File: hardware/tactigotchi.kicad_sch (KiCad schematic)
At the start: 33 parts, among them Q1 BC337, Q2 BC337, SW1 SW_Push, SW10 SW_SPDT, SW2 SW_Push, SW3 SW_Push, SW4 SW_Push, SW5 SW_Push, SW6 SW_Push, SW7 SW_Push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

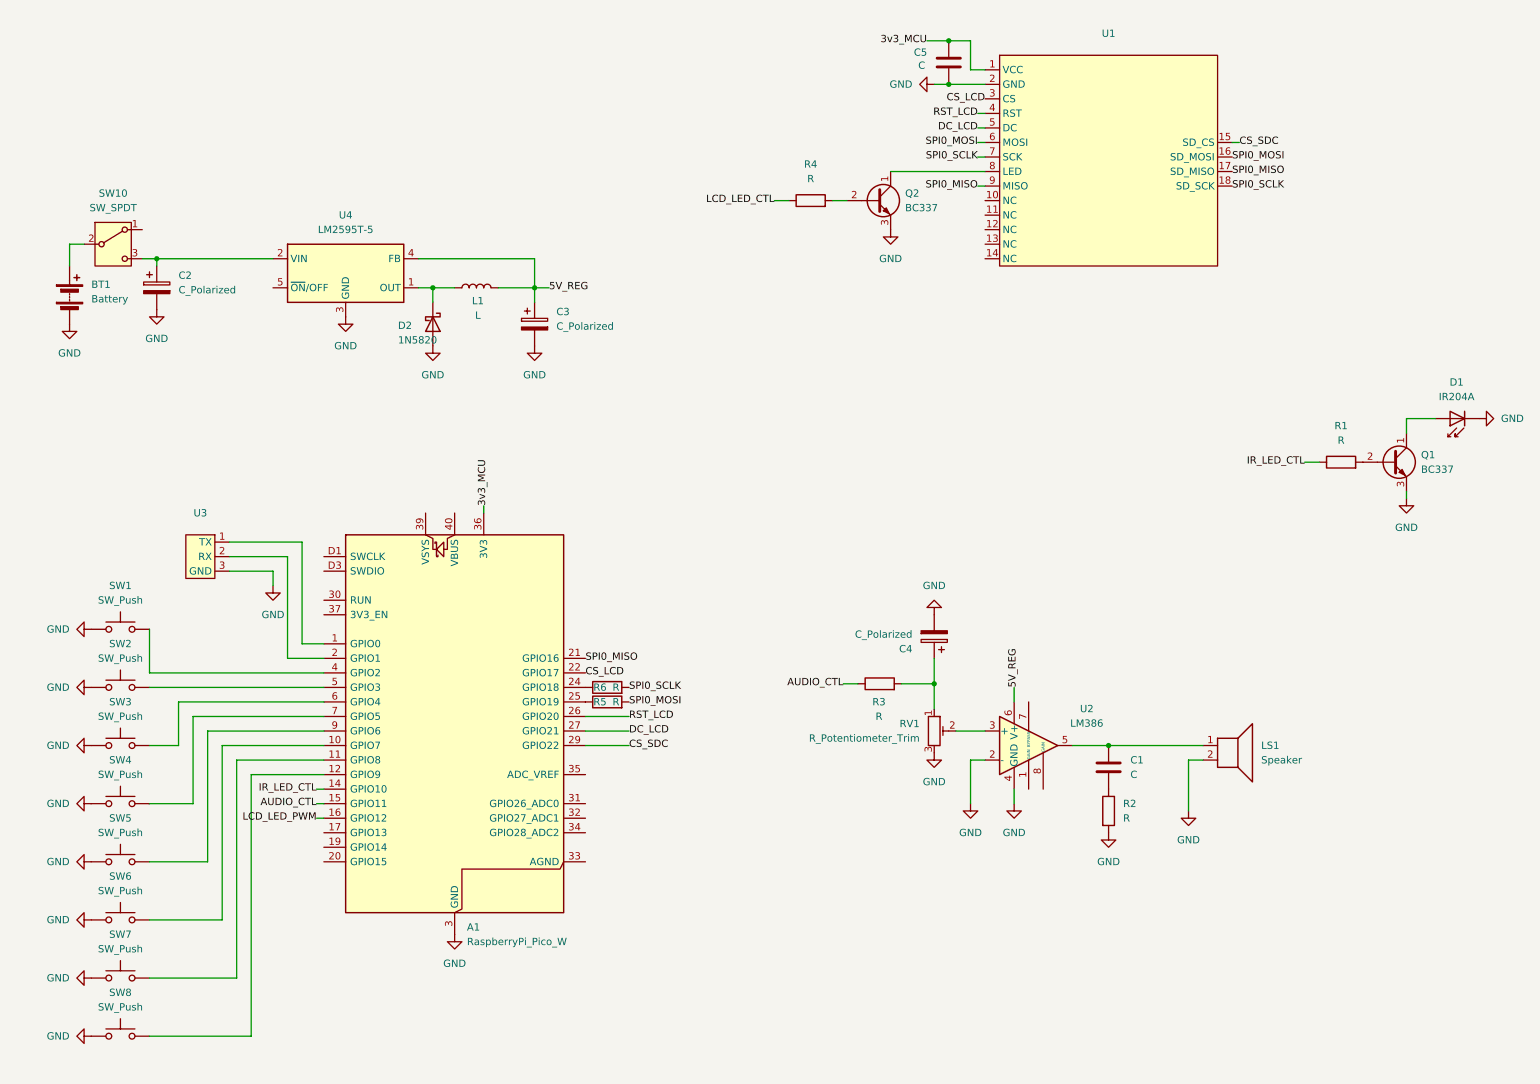
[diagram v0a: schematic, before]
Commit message: Add files via upload
smd schematic drop-in replacements, changes to psu module
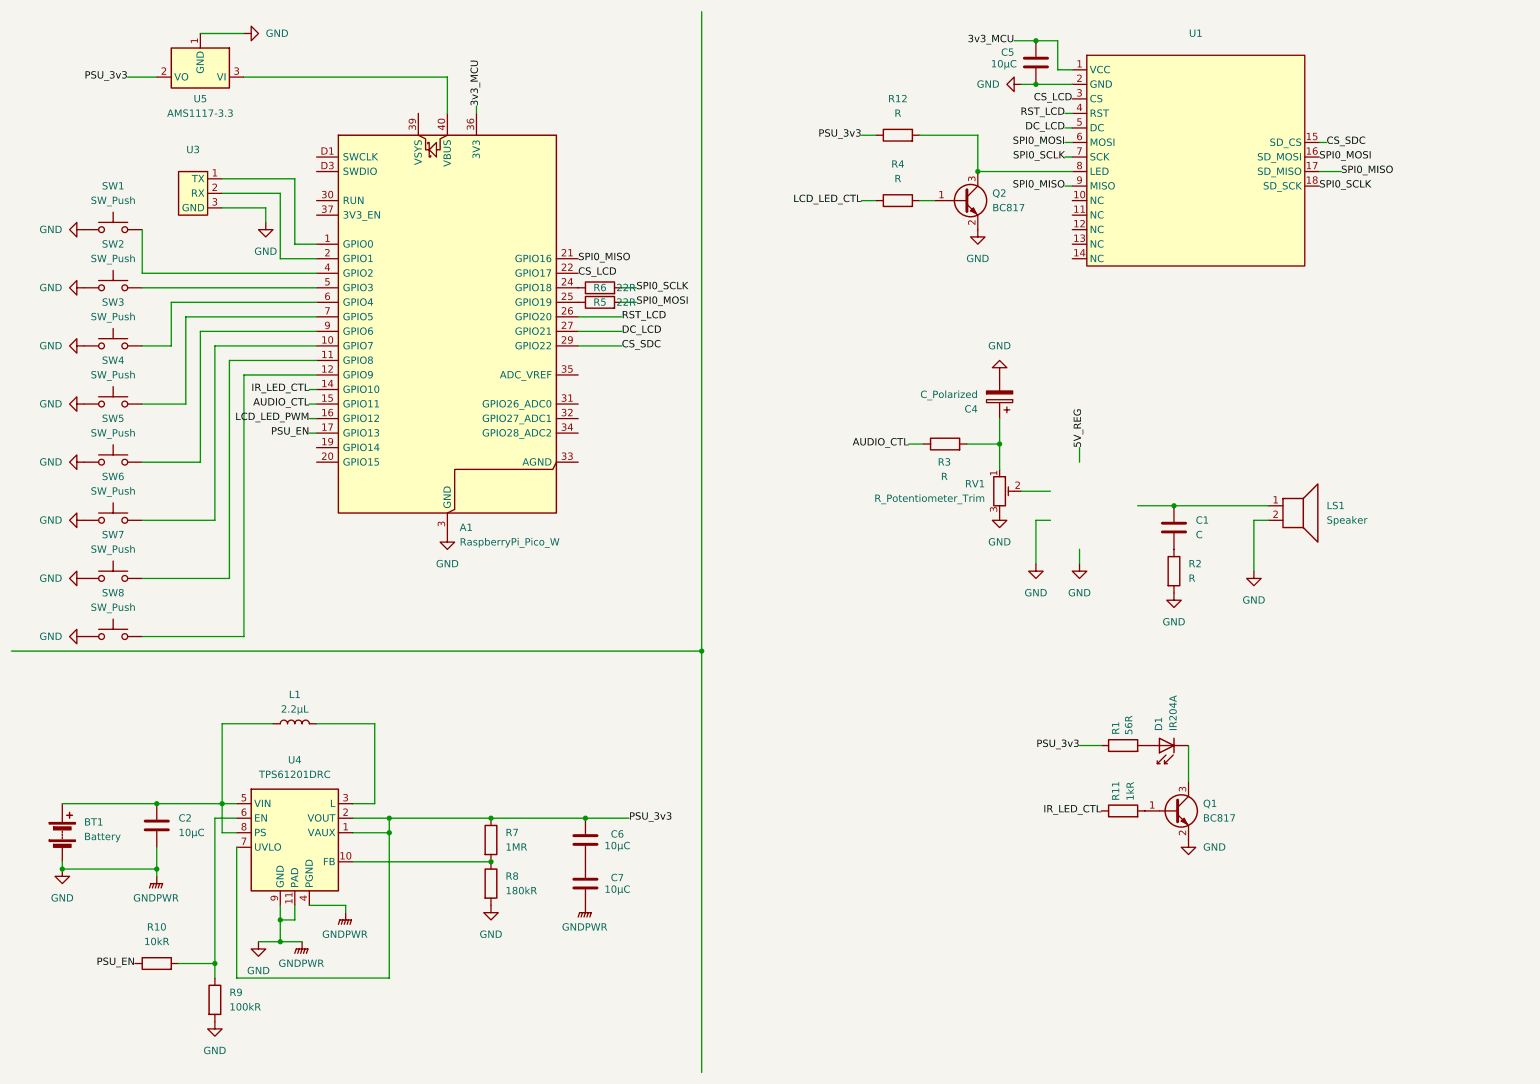
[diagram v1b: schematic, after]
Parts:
- removed C2, C3: C_Polarized, Capacitor_THT:CP_Radial_D5.0mm_P2.50mm, symbol Device:C_Polarized
- removed D2: 1N5820, Diode_THT:D_DO-201AD_P15.24mm_Horizontal, symbol Diode:1N5820
- removed Q1, Q2: BC337, Package_TO_SOT_THT:TO-92_Inline, symbol Transistor_BJT:BC337
- removed SW10: SW_SPDT, Button_Switch_THT:SW_E-Switch_EG1271_SPDT, symbol Switch:SW_SPDT
- removed U2: LM386, Package_DIP:DIP-8_W7.62mm, symbol Amplifier_Audio:LM386
- removed U4: LM2595T-5, Package_TO_SOT_THT:TO-220-5_P3.4x3.7mm_StaggerOdd_Lead3.8mm_Vertical, symbol Regulator_Switching:LM2595T-5
- added C2, C6, C7: 10μC, symbol Device:C
- added Q1, Q2: BC817, Package_TO_SOT_SMD:SOT-23, symbol Transistor_BJT:BC817
- added R10: 10kR, symbol Device:R
- added R11: 1kR, Resistor_THT:R_Axial_DIN0204_L3.6mm_D1.6mm_P5.08mm_Horizontal, symbol Device:R
- added R12: R, Resistor_THT:R_Axial_DIN0204_L3.6mm_D1.6mm_P5.08mm_Horizontal, symbol Device:R
- added R7: 1MR, symbol Device:R
- added R8: 180kR, symbol Device:R
- added R9: 100kR, symbol Device:R
- added U4: TPS61201DRC, Package_SON:Texas_S-PVSON-N10_ThermalVias, symbol Regulator_Switching:TPS61201DRC
- added U5: AMS1117-3.3, Package_TO_SOT_SMD:SOT-223-3_TabPin2, symbol Regulator_Linear:AMS1117-3.3
- C5: value C -> 10μC
- L1: value L -> 2.2μL; footprint Inductor_SMD:L_6.3x6.3_H3 -> (none)
- R1: value R -> 56R
- R5, R6: value R -> 22R
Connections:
- net 5V_REG: no longer L1.2
- net GND: now also C2.2, C7.1, Q1.2 (E), Q2.2 (E), R8.2, R9.2, U4.11 (PAD), U4.4 (PGND), U4.9 (GND), U5.1 (GND); no longer D1.1 (K)
- net IR_LED_CTL: now also R11.1; no longer R1.1
- net at R4.2: now also Q2.1 (B)
- net at U1.8 (LED): now also Q2.3 (C), R12.2
- net at R1.2: now also D1.2 (A)
- net at L1.1: now also BT1.1 (+), C2.1, U4.5 (VIN), U4.8 (PS)
- net PSU_EN: now reaches A1.17 (GPIO13)
- net PSU_EN: now also R10.1
- net at A1.40 (VBUS): now also U5.3 (VI)
- new net: Q1.1 (B), R11.2
- new net: D1.1 (K), Q1.3 (C)
- new net: R10.2, R9.1, U4.6 (EN)
- new net: C6.1, C7.2
- new net: R7.2, R8.1, U4.10 (FB)
- new net: L1.2, U4.3 (L)
- new net PSU_3v3: C6.2, R1.1, R12.1, R7.1, U4.1 (VAUX), U4.2 (VOUT), U4.7 (UVLO), U5.2 (VO)
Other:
- moved on the sheet: A1, BT1, C1, C4, C5, D1, LS1, R1, R2, R3, R4, R5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

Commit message: Add files via upload
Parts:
- removed C1: C, Capacitor_THT:CP_Radial_D5.0mm_P2.50mm, symbol Device:C
- removed C4: C_Polarized, Capacitor_THT:CP_Radial_D5.0mm_P2.50mm, symbol Device:C_Polarized
- removed R3: R, Resistor_THT:R_Axial_DIN0204_L3.6mm_D1.6mm_P5.08mm_Horizontal, symbol Device:R
- removed RV1: R_Potentiometer_Trim, Potentiometer_THT:Potentiometer_Piher_PT-10-H01_Horizontal, symbol Device:R_Potentiometer_Trim
- added C10, C8, C9: .1μC, symbol Device:C
- added C11: 22μC, symbol Device:C
- added C12: 10μC, symbol Device:C
- added R14: 22R, symbol Device:R
- added U2: PAM8302AAD, symbol Amplifier_Audio:PAM8302AAD
- R2: value R -> 1kR
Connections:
- net LCD_LED_PWM is gone; now on net LCD_LED_CTL: A1.16 (GPIO12)
- net AUDIO_CTL: now also A1.31 (GPIO26_ADC0), C8.1; no longer A1.15 (GPIO11)
- net GND: now also C10.1, C11.2, C12.2, C9.2, U2.7 (GND); no longer LS1.2
- net PSU_3v3: now also C10.2, C11.1, U2.6 (VDD)
- net SPI0_MISO: now also R14.2; no longer U1.17 (SD_MISO)
- net at A1.40 (VBUS), U5.3 (VI): now also C12.1
- net AUDIO_EN: now reaches R2.1
- net AUDIO_EN: now also A1.15 (GPIO11), U2.1 (~{SD})
- net at LS1.1: now also U2.5 (OUT+)
- new net: C8.2, U2.3 (IN+)
- new net: C9.1, U2.4 (IN-)
- new net: LS1.2, U2.8 (OUT-)
- new net: R14.1, U1.17 (SD_MISO)
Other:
- moved on the sheet: D1, LS1, Q1, R1, R11

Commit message: beginnings of pcb layout
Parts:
- C10, C11, C12, C2, C5, C6, C7, C8, C9: footprint (none) -> Capacitor_SMD:C_1206_3216Metric
- L1: footprint (none) -> Inductor_SMD:L_1206_3216Metric
- R1, R11, R12, R2: footprint Resistor_THT:R_Axial_DIN0204_L3.6mm_D1.6mm_P5.08mm_Horizontal -> Resistor_SMD:R_1206_3216Metric
- R10, R14, R5, R6, R7, R8, R9: footprint (none) -> Resistor_SMD:R_1206_3216Metric
- R4: value R -> 22R; footprint Resistor_THT:R_Axial_DIN0204_L3.6mm_D1.6mm_P5.08mm_Horizontal -> Resistor_SMD:R_1206_3216Metric
- SW1, SW2, SW3, SW4, SW5, SW6, SW7, SW8: footprint Button_Switch_THT:SW_PUSH_6mm -> Button_Switch_SMD:SW_SPST_PTS645
- U2: footprint (none) -> Package_SO:SOIC-8-1EP_3.9x4.9mm_P1.27mm_EP2.41x3.3mm
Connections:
- net PSU_3v3: now also A1.39 (VSYS)
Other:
- moved on the sheet: LS1
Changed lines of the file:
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@@
 	(wire
 		(pts
+			(xy 196.85 102.87) (xy 196.85 104.14)
+		)
+		(stroke
+			(width 0)
+			(type default)
+		)
+	)
+	(wire
+		(pts
 			(xy 196.85 38.1) (xy 198.12 38.1)
 		)
@@
 	(wire
 		(pts
-			(xy 201.93 105.41) (xy 196.85 105.41)
+			(xy 191.77 102.87) (xy 196.85 102.87)
+		)
+		(stroke
+			(width 0)
+			(type default)
+		)
+	)
+	(wire
+		(pts
+			(xy 205.74 106.68) (xy 196.85 106.68)
 		)
 		(stroke
@@
 	(wire
 		(pts
-			(xy 191.77 102.87) (xy 201.93 102.87)
+			(xy 196.85 104.14) (xy 205.74 104.14)
 		)
 		(stroke
@@
 	(wire
 		(pts
-			(xy 196.85 105.41) (xy 196.85 107.95)
+			(xy 196.85 106.68) (xy 196.85 107.95)
 		)
 		(stroke
@@
 		)
 	)
+	(label "PSU_3v3"
+		(at 83.82 30.48 90)
+		(effects
+			(font
+				(size 1.27 1.27)
+			)
+			(justify left)
+		)
+	)
 	(label "SPI0_SCLK"
 		(at 196.85 38.1 180)
@@
 			)
 		)
-		(property "Footprint" ""
+		(property "Footprint" "Package_SO:SOIC-8-1EP_3.9x4.9mm_P1.27mm_EP2.41x3.3mm"
 			(at 181.61 107.95 0)
 			(effects
@@
 			)
 		)
-		(property "Footprint" "Button_Switch_THT:SW_PUSH_6mm"
+		(property "Footprint" "Button_Switch_SMD:SW_SPST_PTS645"
 			(at 30.48 55.88 0)
 			(effects
@@
 			)
 		)
-		(property "Footprint" "Button_Switch_THT:SW_PUSH_6mm"
+		(property "Footprint" "Button_Switch_SMD:SW_SPST_PTS645"
 			(at 30.48 116.84 0)
 			(effects
@@
 			)
 		)
-		(property "Footprint" ""
+		(property "Footprint" "Resistor_SMD:R_1206_3216Metric"
 			(at 115.57 62.738 90)
 			(effects
@@
 			)
 		)
-		(property "Value" "R"
+		(property "Value" "22R"
 			(at 167.64 41.91 90)
 			(effects
@@
 			)
 		)
-		(property "Footprint" "Resistor_THT:R_Axial_DIN0204_L3.6mm_D1.6mm_P5.08mm_Horizontal"
+		(property "Footprint" "Resistor_SMD:R_1206_3216Metric"
 			(at 167.64 47.498 90)
 			(effects
@@
 			)
 		)
-		(property "Footprint" ""
+		(property "Footprint" "Resistor_SMD:R_1206_3216Metric"
 			(at 46.482 185.42 90)
 			(effects
@@
 			)
 		)
-		(property "Footprint" "Resistor_THT:R_Axial_DIN0204_L3.6mm_D1.6mm_P5.08mm_Horizontal"
+		(property "Footprint" "Resistor_SMD:R_1206_3216Metric"
 			(at 252.73 113.538 90)
 			(effects
@@
 			)
 		)
-		(property "Footprint" ""
+		(property "Footprint" "Capacitor_SMD:C_1206_3216Metric"
 			(at 171.45 101.9048 0)
 			(effects
@@
 			)
 		)
-		(property "Footprint" ""
+		(property "Footprint" "Resistor_SMD:R_1206_3216Metric"
 			(at 245.11 42.418 90)
 			(effects
@@
 			)
 		)
-		(property "Footprint" "Resistor_THT:R_Axial_DIN0204_L3.6mm_D1.6mm_P5.08mm_Horizontal"
+		(property "Footprint" "Resistor_SMD:R_1206_3216Metric"
 			(at 252.73 102.108 90)
 			(effects
@@
 			)
 		)
-		(property "Footprint" ""
+		(property "Footprint" "Capacitor_SMD:C_1206_3216Metric"
 			(at 33.3248 15.24 0)
 			(effects
@@
 			)
 		)
-		(property "Footprint" ""
+		(property "Footprint" "Capacitor_SMD:C_1206_3216Metric"
 			(at 112.0648 161.29 0)
 			(effects
@@
 			)
 		)
-		(property "Footprint" ""
+		(property "Footprint" "Capacitor_SMD:C_1206_3216Metric"
 			(at 112.0648 153.67 0)
 			(effects
@@
 			)
 		)
-		(property "Footprint" "Button_Switch_THT:SW_PUSH_6mm"
+		(property "Footprint" "Button_Switch_SMD:SW_SPST_PTS645"
 			(at 30.48 76.2 0)
 			(effects
@@
 			)
 		)
-		(property "Footprint" "Button_Switch_THT:SW_PUSH_6mm"
+		(property "Footprint" "Button_Switch_SMD:SW_SPST_PTS645"
 			(at 30.48 96.52 0)
 			(effects
@@
 			)
 		)
-		(property "Footprint" ""
+		(property "Footprint" "Resistor_SMD:R_1206_3216Metric"
 			(at 38.1 180.848 90)
 			(effects
@@
 			)
 		)
-		(property "Footprint" "Button_Switch_THT:SW_PUSH_6mm"
+		(property "Footprint" "Button_Switch_SMD:SW_SPST_PTS645"
 			(at 30.48 45.72 0)
 			(effects
@@
 			)
 		)
-		(property "Footprint" ""
+		(property "Footprint" "Capacitor_SMD:C_1206_3216Metric"
 			(at 39.0652 158.75 0)
 			(effects
@@
 			)
 		)
-		(property "Footprint" ""
+		(property "Footprint" "Resistor_SMD:R_1206_3216Metric"
 			(at 94.742 165.1 90)
 			(effects
@@
 			)
 		)
-		(property "Footprint" "Button_Switch_THT:SW_PUSH_6mm"
+		(property "Footprint" "Button_Switch_SMD:SW_SPST_PTS645"
 			(at 30.48 66.04 0)
 			(effects
@@
 			)
 		)
-		(property "Footprint" ""
+		(property "Footprint" "Resistor_SMD:R_1206_3216Metric"
 			(at 94.742 157.48 90)
 			(effects
@@
 			)
 		)
-		(property "Footprint" ""
+		(property "Footprint" "Capacitor_SMD:C_1206_3216Metric"
 			(at 156.21 108.9152 0)
 			(effects
@@
 			)
 		)
-		(property "Footprint" ""
+		(property "Footprint" "Inductor_SMD:L_1206_3216Metric"
 			(at 62.23 137.16 0)
 			(effects
@@
 			)
 		)
-		(property "Footprint" "Resistor_THT:R_Axial_DIN0204_L3.6mm_D1.6mm_P5.08mm_Horizontal"
+		(property "Footprint" "Resistor_SMD:R_1206_3216Metric"
 			(at 167.64 36.068 90)
 			(effects
@@
 			)
 		)
-		(property "Footprint" "Resistor_THT:R_Axial_DIN0204_L3.6mm_D1.6mm_P5.08mm_Horizontal"
+		(property "Footprint" "Resistor_SMD:R_1206_3216Metric"
 			(at 165.862 121.92 90)
 			(effects
@@
 			)
 		)
-		(property "Footprint" "Button_Switch_THT:SW_PUSH_6mm"
+		(property "Footprint" "Button_Switch_SMD:SW_SPST_PTS645"
 			(at 30.48 86.36 0)
 			(effects
@@
 			)
 		)
-		(property "Footprint" ""
+		(property "Footprint" "Capacitor_SMD:C_1206_3216Metric"
 			(at 192.7352 25.4 0)
 			(effects
@@
 			)
 		)
-		(property "Footprint" ""
+		(property "Footprint" "Capacitor_SMD:C_1206_3216Metric"
 			(at 59.3852 31.75 0)
 			(effects
@@
 			)
 		)
-		(property "Footprint" ""
+		(property "Footprint" "Resistor_SMD:R_1206_3216Metric"
 			(at 115.57 65.278 90)
 			(effects
@@
 	(symbol
 		(lib_id "Device:Speaker")
-		(at 207.01 102.87 0)
+		(at 210.82 104.14 0)
 		(unit 1)
 		(exclude_from_sim no)
@@
 		(fields_autoplaced yes)
 		(property "Reference" "LS1"
-			(at 212.09 102.8699 0)
+			(at 215.9 104.1399 0)
 			(effects
 				(font
@@
 		)
 		(property "Value" "Speaker"
-			(at 212.09 105.4099 0)
+			(at 215.9 106.6799 0)
 			(effects
 				(font
@@
 		)
 		(property "Footprint" "Buzzer_Beeper:Buzzer_12x9.5RM7.6"
-			(at 207.01 107.95 0)
+			(at 210.82 109.22 0)
 			(effects
 				(font
@@
 		)
 		(property "Datasheet" "~"
-			(at 206.756 104.14 0)
+			(at 210.566 105.41 0)
 			(effects
 				(font
@@
 		)
 		(property "Description" "Speaker"
-			(at 207.01 102.87 0)
+			(at 210.82 104.14 0)
 			(effects
 				(font
@@
 			)
 		)
-		(property "Footprint" ""
+		(property "Footprint" "Capacitor_SMD:C_1206_3216Metric"
 			(at 181.61 85.3948 0)
 			(effects
@@
 			)
 		)
-		(property "Footprint" "Button_Switch_THT:SW_PUSH_6mm"
+		(property "Footprint" "Button_Switch_SMD:SW_SPST_PTS645"
 			(at 30.48 106.68 0)
 			(effects

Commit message: Add files via upload
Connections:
- net GND: now also U1.10 (NC), U1.11 (NC), U1.12 (NC), U1.13 (NC), U1.14 (NC)
